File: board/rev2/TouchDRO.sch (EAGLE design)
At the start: 27 parts

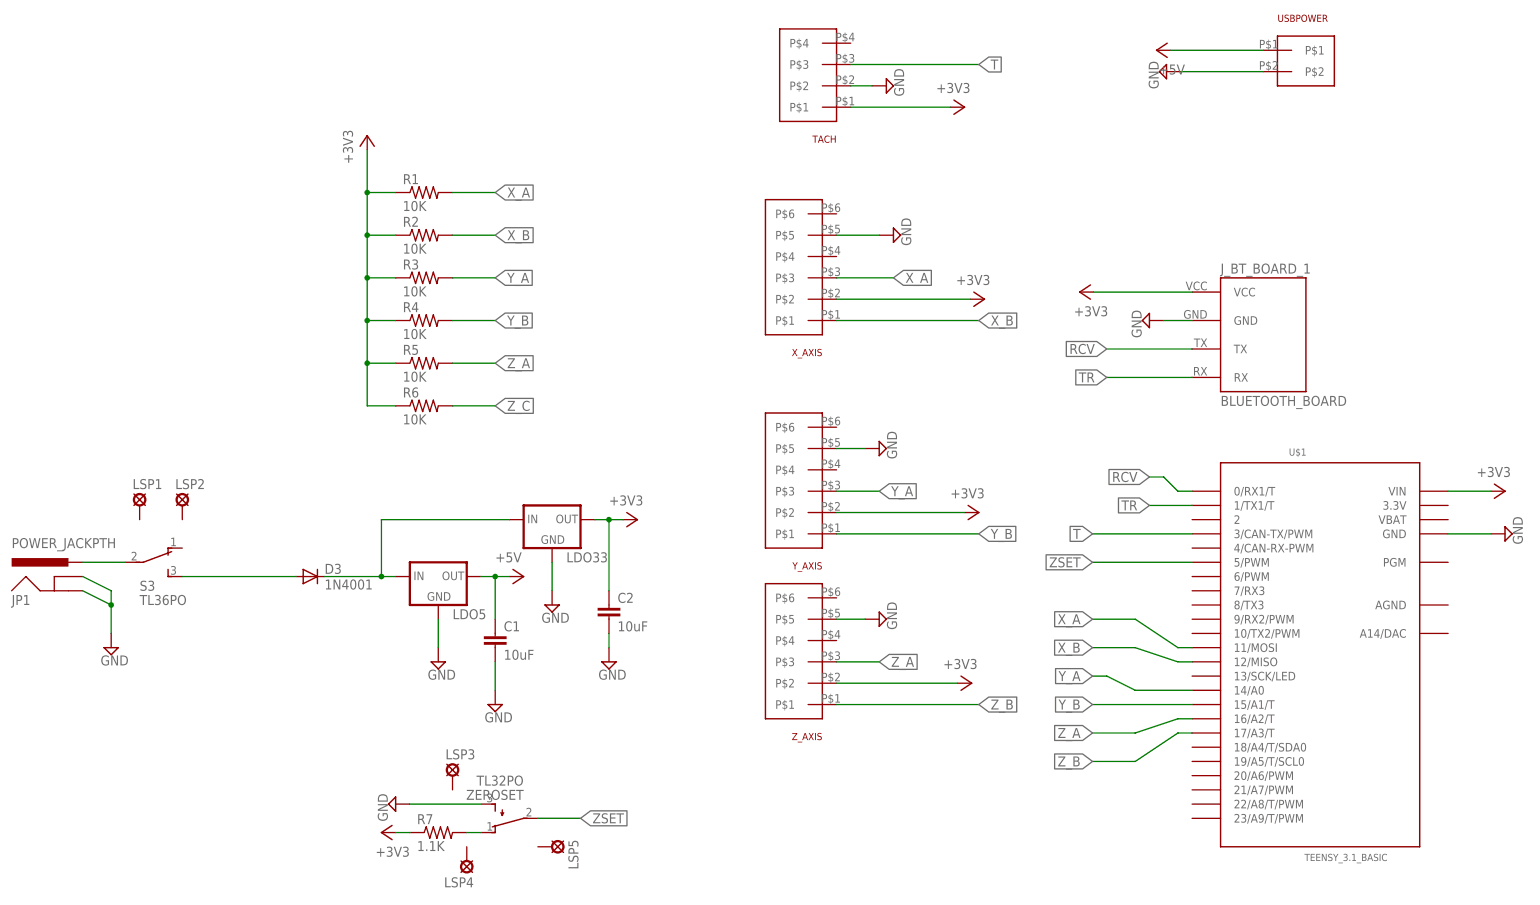
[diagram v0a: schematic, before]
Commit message: adding rev2 dependencies and updates to the rev2 board
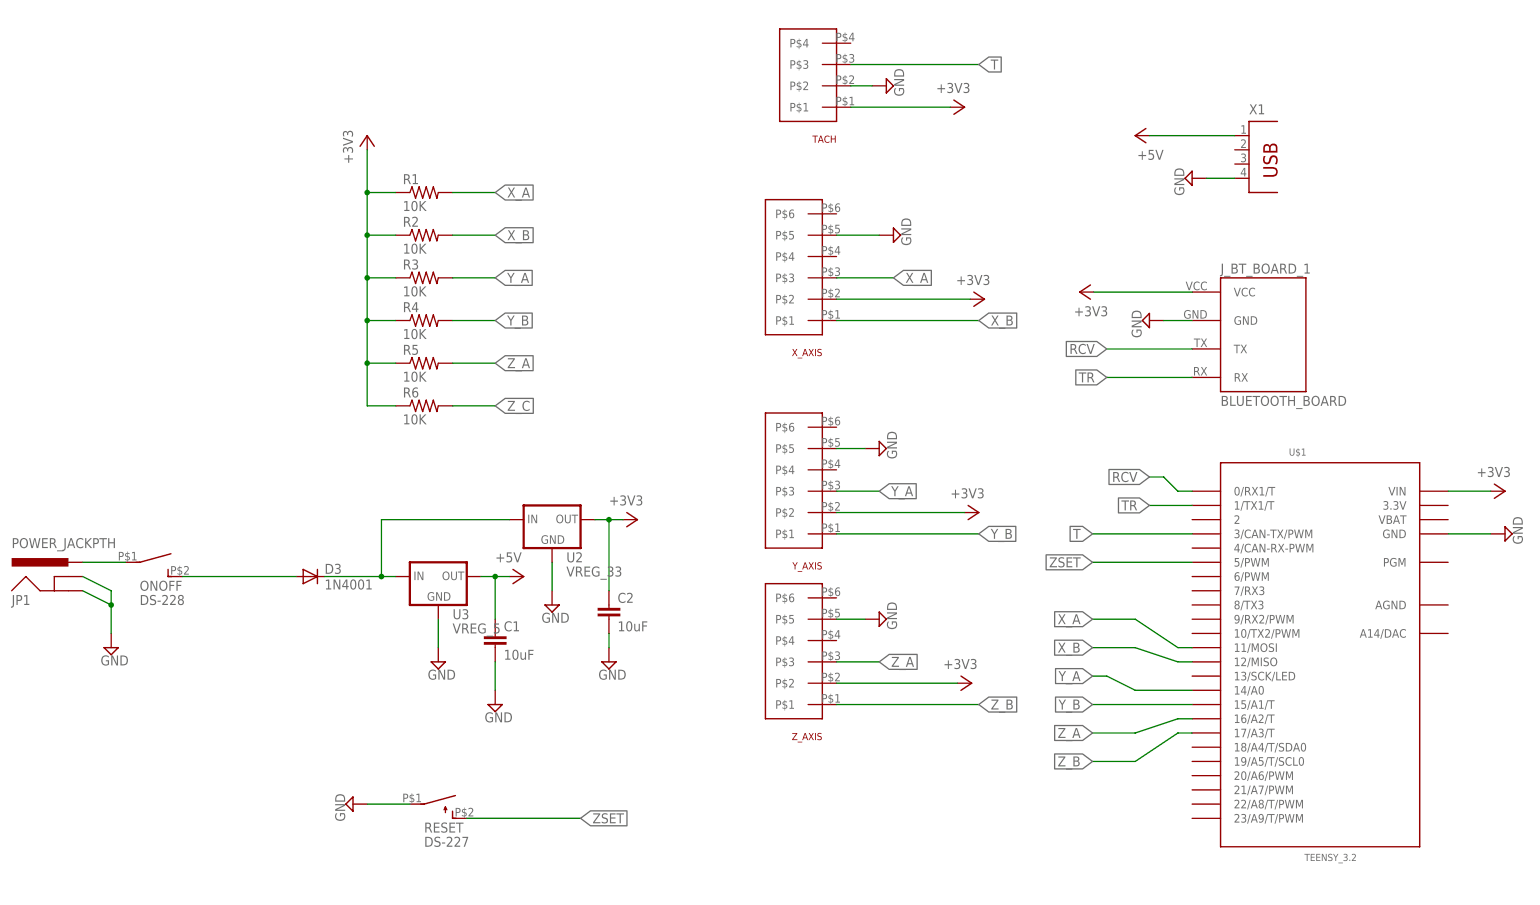
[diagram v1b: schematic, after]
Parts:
- removed LDO33, LDO5: (no value), SparkFun-PowerIC:V_REG_78XXSINK
- removed LSP1, LSP2, LSP3, LSP4, LSP5: LSP13, solpad:LSP13
- removed R7: 1.1K, SparkFun-Passives:RESISTOREZ
- removed S3: TL36PO, switch:TL36PO
- removed USBPOWER: KF2510_2PIN, KF2510:KF2510_2PIN
- removed ZEROSET: TL32PO, switch:TL32PO
- added ONOFF: DS-228, Switches:DS-228
- added RESET: DS-227, Switches:DS-227
- added U2: VREG_33, regulators:VREG_33
- added U3: VREG_5, regulators:VREG_5
- added X1: (no value), con-berg:PN87520
- U$1: value TEENSY_3.1_BASIC -> TEENSY_3.2
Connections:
- removed net N$2: R7.2, ZEROSET.O
- net +3V3: now also U2.OUT; no longer LDO33.OUT, R7.1
- net +5V: now also U3.OUT, X1.1; no longer LDO5.OUT, USBPOWER.P$1
- net D1: now also U2.IN, U3.IN; no longer LDO33.IN, LDO5.IN
- net GND: now also RESET.P, U2.GND, U3.GND, X1.4; no longer LDO33.GND, LDO5.GND, USBPOWER.P$2, ZEROSET.S
- net N$6: now also ONOFF.P; no longer S3.P
- net ONOFF: now also ONOFF.S; no longer S3.S
- net ZSET: now also RESET.S; no longer ZEROSET.P
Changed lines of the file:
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@@
 <part name="SUPPLY2" library="supply2" deviceset="GND" device=""/>
 <part name="J_BT_BOARD_1" library="Bluetooth HC-05" deviceset="BLUETOOTH_BOARD" device=""/>
-<part name="U$1" library="Teensy_3_Series_Board_v1.0" deviceset="TEENSY_3.1_BASIC" device=""/>
+<part name="U$1" library="Teensy_3_Series_Board_v1.0" deviceset="TEENSY_3.1_BASIC" device="" value="TEENSY_3.2"/>
 <part name="SUPPLY5" library="supply2" deviceset="GND" device=""/>
 <part name="SUPPLY7" library="supply2" deviceset="GND" device=""/>
@@
 <part name="SUPPLY16" library="supply2" deviceset="GND" device=""/>
 <part name="SUPPLY18" library="supply2" deviceset="GND" device=""/>
-<part name="USBPOWER" library="KF2510" deviceset="KF2510_2PIN" device=""/>
 <part name="SUPPLY20" library="supply2" deviceset="GND" device=""/>
 <part name="P+2" library="supply1" deviceset="+5V" device=""/>
@@
 <part name="C2" library="SparkFun-Passives" deviceset="CAP" device="EZ" value="10uF"/>
 <part name="SUPPLY1" library="supply2" deviceset="GND" device=""/>
-<part name="LDO5" library="SparkFun-PowerIC" deviceset="V_REG_78XX" device="SINK"/>
-<part name="LDO33" library="SparkFun-PowerIC" deviceset="V_REG_78XX" device="SINK"/>
 <part name="+3V1" library="supply1" deviceset="+3V3" device=""/>
 <part name="+3V2" library="supply1" deviceset="+3V3" device=""/>
 <part name="P+1" library="supply1" deviceset="+5V" device=""/>
-<part name="ZEROSET" library="switch" deviceset="TL32PO" device=""/>
-<part name="S3" library="switch" deviceset="TL36PO" device=""/>
 <part name="SUPPLY3" library="supply2" deviceset="GND" device=""/>
-<part name="+3V7" library="supply1" deviceset="+3V3" device=""/>
 <part name="R1" library="SparkFun-Passives" deviceset="RESISTOR" device="EZ" value="10K"/>
 <part name="R2" library="SparkFun-Passives" deviceset="RESISTOR" device="EZ" value="10K"/>
@@
 <part name="R5" library="SparkFun-Passives" deviceset="RESISTOR" device="EZ" value="10K"/>
 <part name="R6" library="SparkFun-Passives" deviceset="RESISTOR" device="EZ" value="10K"/>
-<part name="R7" library="SparkFun-Passives" deviceset="RESISTOR" device="EZ" value="1.1K"/>
-<part name="LSP1" library="solpad" deviceset="LSP13" device=""/>
-<part name="LSP2" library="solpad" deviceset="LSP13" device=""/>
-<part name="LSP3" library="solpad" deviceset="LSP13" device=""/>
-<part name="LSP4" library="solpad" deviceset="LSP13" device=""/>
-<part name="LSP5" library="solpad" deviceset="LSP13" device=""/>
+<part name="RESET" library="Switches" deviceset="DS-227" device=""/>
+<part name="ONOFF" library="Switches" deviceset="DS-228" device=""/>
+<part name="X1" library="con-berg" deviceset="PN87520" device=""/>
+<part name="U2" library="regulators" deviceset="VREG_33" device=""/>
+<part name="U3" library="regulators" deviceset="VREG_5" device=""/>
 </parts>
 <sheets>
@@
 <instance part="SUPPLY16" gate="GND" x="-68.58" y="-27.94"/>
 <instance part="SUPPLY18" gate="GND" x="-78.74" y="-20.32"/>
-<instance part="USBPOWER" gate="G$1" x="71.12" y="91.44"/>
-<instance part="SUPPLY20" gate="GND" x="51.308" y="85.09" rot="R270"/>
+<instance part="SUPPLY20" gate="GND" x="55.88" y="66.04" rot="R270"/>
 <instance part="P+2" gate="1" x="-63.5" y="-5.08" rot="R270"/>
 <instance part="+3V3" gate="G$1" x="-43.18" y="5.08" rot="R270"/>
@@
 <instance part="C2" gate="G$1" x="-48.26" y="-12.7"/>
 <instance part="SUPPLY1" gate="GND" x="-48.26" y="-20.32"/>
-<instance part="LDO5" gate="G$1" x="-78.74" y="-5.08"/>
-<instance part="LDO33" gate="G$1" x="-58.42" y="5.08"/>
 <instance part="+3V1" gate="G$1" x="35.814" y="45.72" rot="R90"/>
 <instance part="+3V2" gate="G$1" x="-91.44" y="73.66"/>
-<instance part="P+1" gate="1" x="49.53" y="88.9" rot="R90"/>
-<instance part="ZEROSET" gate="BEF1" x="-66.04" y="-48.26" rot="R90"/>
-<instance part="S3" gate="BEF1" x="-129.54" y="-2.54" rot="R270"/>
-<instance part="SUPPLY3" gate="GND" x="-86.36" y="-45.72" rot="R270"/>
-<instance part="+3V7" gate="G$1" x="-88.9" y="-50.8" rot="R90"/>
+<instance part="P+1" gate="1" x="45.72" y="73.66" rot="R90"/>
+<instance part="SUPPLY3" gate="GND" x="-93.98" y="-45.72" rot="R270"/>
 <instance part="R1" gate="G$1" x="-81.28" y="63.5"/>
 <instance part="R2" gate="G$1" x="-81.28" y="55.88"/>
@@
 <instance part="R5" gate="G$1" x="-81.28" y="33.02"/>
 <instance part="R6" gate="G$1" x="-81.28" y="25.4"/>
-<instance part="R7" gate="G$1" x="-78.74" y="-50.8"/>
-<instance part="LSP1" gate="1" x="-132.08" y="7.62"/>
-<instance part="LSP2" gate="1" x="-124.46" y="7.62"/>
-<instance part="LSP3" gate="1" x="-76.2" y="-40.64"/>
-<instance part="LSP4" gate="1" x="-73.66" y="-55.88" rot="R180"/>
-<instance part="LSP5" gate="1" x="-58.42" y="-53.34" rot="R270"/>
+<instance part="RESET" gate="G$1" x="-78.74" y="-45.72" rot="R270"/>
+<instance part="ONOFF" gate="G$1" x="-129.54" y="-2.54" rot="R270"/>
+<instance part="X1" gate="G$1" x="66.04" y="68.58"/>
+<instance part="U2" gate="G$1" x="-58.42" y="5.08"/>
+<instance part="U3" gate="G$1" x="-78.74" y="-5.08"/>
 </instances>
 <busses>
@@
 </segment>
 <segment>
-<pinref part="USBPOWER" gate="G$1" pin="P$2"/>
-<wire x1="68.58" y1="85.09" x2="53.848" y2="85.09" width="0.1524" layer="91"/>
-<pinref part="SUPPLY20" gate="GND" pin="GND"/>
-</segment>
-<segment>
 <pinref part="SUPPLY1" gate="GND" pin="GND"/>
 <pinref part="C2" gate="G$1" pin="2"/>
@@
 </segment>
 <segment>
-<pinref part="LDO33" gate="G$1" pin="GND"/>
 <pinref part="SUPPLY15" gate="GND" pin="GND"/>
 <wire x1="-58.42" y1="-2.54" x2="-58.42" y2="-7.62" width="0.1524" layer="91"/>
+<pinref part="U2" gate="G$1" pin="GND"/>
 </segment>
 <segment>
 <pinref part="SUPPLY18" gate="GND" pin="GND"/>
-<pinref part="LDO5" gate="G$1" pin="GND"/>
 <wire x1="-78.74" y1="-17.78" x2="-78.74" y2="-12.7" width="0.1524" layer="91"/>
-</segment>
-<segment>
-<pinref part="ZEROSET" gate="BEF1" pin="S"/>
-<wire x1="-71.12" y1="-45.72" x2="-83.82" y2="-45.72" width="0.1524" layer="91"/>
+<pinref part="U3" gate="G$1" pin="GND"/>
+</segment>
+<segment>
 <pinref part="SUPPLY3" gate="GND" pin="GND"/>
+<pinref part="RESET" gate="G$1" pin="P"/>
+<wire x1="-91.44" y1="-45.72" x2="-83.82" y2="-45.72" width="0.1524" layer="91"/>
+</segment>
+<segment>
+<pinref part="X1" gate="G$1" pin="4"/>
+<wire x1="63.5" y1="66.04" x2="58.42" y2="66.04" width="0.1524" layer="91"/>
+<pinref part="SUPPLY20" gate="GND" pin="GND"/>
 </segment>
 </net>
@@
 <pinref part="JP1" gate="G$1" pin="PWR"/>
 <wire x1="-142.24" y1="-2.54" x2="-134.62" y2="-2.54" width="0.1524" layer="91"/>
-<pinref part="S3" gate="BEF1" pin="P"/>
+<pinref part="ONOFF" gate="G$1" pin="P"/>
 </segment>
 </net>
@@
 <pinref part="D3" gate="G$1" pin="A"/>
 <wire x1="-124.46" y1="-5.08" x2="-104.14" y2="-5.08" width="0.1524" layer="91"/>
-<pinref part="S3" gate="BEF1" pin="S"/>
+<pinref part="ONOFF" gate="G$1" pin="S"/>
 </segment>
 </net>
 <net name="+5V" class="0">
 <segment>
-<pinref part="LDO5" gate="G$1" pin="OUT"/>
 <pinref part="P+2" gate="1" pin="+5V"/>
 <wire x1="-71.12" y1="-5.08" x2="-68.58" y2="-5.08" width="0.1524" layer="91"/>
@@
 <pinref part="C1" gate="G$1" pin="1"/>
 <wire x1="-68.58" y1="-5.08" x2="-68.58" y2="-12.7" width="0.1524" layer="91"/>
-</segment>
-<segment>
-<pinref part="USBPOWER" gate="G$1" pin="P$1"/>
-<wire x1="68.58" y1="88.9" x2="52.07" y2="88.9" width="0.1524" layer="91"/>
+<pinref part="U3" gate="G$1" pin="OUT"/>
+</segment>
+<segment>
+<pinref part="X1" gate="G$1" pin="1"/>
+<wire x1="48.26" y1="73.66" x2="63.5" y2="73.66" width="0.1524" layer="91"/>
 <pinref part="P+1" gate="1" pin="+5V"/>
 </segment>
@@
 </segment>
 <segment>
-<pinref part="LDO33" gate="G$1" pin="OUT"/>
 <pinref part="+3V3" gate="G$1" pin="+3V3"/>
 <wire x1="-50.8" y1="5.08" x2="-48.26" y2="5.08" width="0.1524" layer="91"/>
@@
 <pinref part="C2" gate="G$1" pin="1"/>
 <wire x1="-48.26" y1="5.08" x2="-48.26" y2="-7.62" width="0.1524" layer="91"/>
+<pinref part="U2" gate="G$1" pin="OUT"/>
 </segment>
 <segment>
@@
 <pinref part="R6" gate="G$1" pin="1"/>
 </segment>
-<segment>
-<pinref part="+3V7" gate="G$1" pin="+3V3"/>
-<wire x1="-86.36" y1="-50.8" x2="-83.82" y2="-50.8" width="0.1524" layer="91"/>
-<pinref part="R7" gate="G$1" pin="1"/>
-</segment>
 </net>
 <net name="D1" class="0">
 <segment>
-<pinref part="LDO5" gate="G$1" pin="IN"/>
 <wire x1="-88.9" y1="-5.08" x2="-86.36" y2="-5.08" width="0.1524" layer="91"/>
 <wire x1="-88.9" y1="-5.08" x2="-88.9" y2="5.08" width="0.1524" layer="91"/>
-<pinref part="LDO33" gate="G$1" pin="IN"/>
 <wire x1="-88.9" y1="5.08" x2="-66.04" y2="5.08" width="0.1524" layer="91"/>
 <pinref part="D3" gate="G$1" pin="C"/>
 <wire x1="-99.06" y1="-5.08" x2="-88.9" y2="-5.08" width="0.1524" layer="91"/>
 <junction x="-88.9" y="-5.08"/>
+<pinref part="U2" gate="G$1" pin="IN"/>
+<pinref part="U3" gate="G$1" pin="IN"/>
 </segment>
 </net>
@@
 </segment>
 <segment>
-<pinref part="ZEROSET" gate="BEF1" pin="P"/>
-<wire x1="-60.96" y1="-48.26" x2="-53.34" y2="-48.26" width="0.1524" layer="91"/>
+<wire x1="-73.66" y1="-48.26" x2="-53.34" y2="-48.26" width="0.1524" layer="91"/>
 <label x="-53.34" y="-48.26" size="1.778" layer="95" xref="yes"/>
-</segment>
-</net>
-<net name="N$2" class="0">
-<segment>
-<pinref part="ZEROSET" gate="BEF1" pin="O"/>
-<wire x1="-73.66" y1="-50.8" x2="-71.12" y2="-50.8" width="0.1524" layer="91"/>
-<pinref part="R7" gate="G$1" pin="2"/>
-</segment>
-</net>
+<pinref part="RESET" gate="G$1" pin="S"/>
+</segment>
+</net>

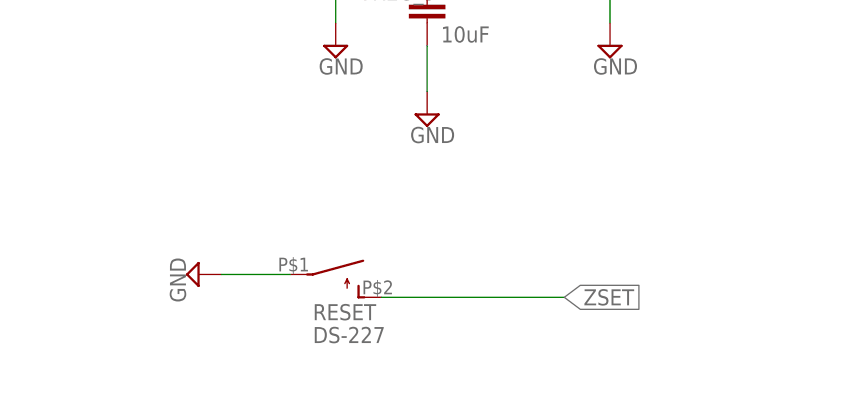
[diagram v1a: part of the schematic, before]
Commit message: tweaks to board and layout. added dxf output of board layout
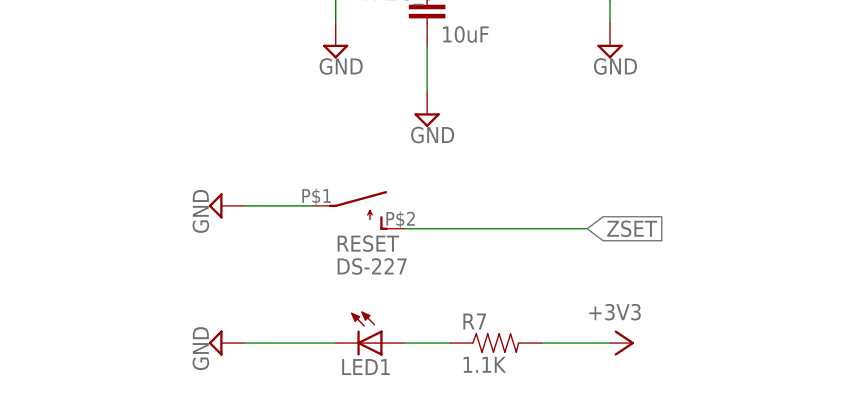
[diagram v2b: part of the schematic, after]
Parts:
- added LED1: (no value), led:LED3MM
- added R7: 1.1K, SparkFun-Passives:RESISTOREZ
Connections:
- new net N$1: LED1.A, R7.1
- net +3V3: now also R7.2
- net GND: now also LED1.C
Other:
- moved on the sheet: RESET
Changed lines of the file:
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@@
 <part name="U2" library="regulators" deviceset="VREG_33" device=""/>
 <part name="U3" library="regulators" deviceset="VREG_5" device=""/>
+<part name="LED1" library="led" deviceset="LED" device="3MM"/>
+<part name="SUPPLY4" library="supply2" deviceset="GND" device=""/>
+<part name="+3V7" library="supply1" deviceset="+3V3" device=""/>
+<part name="R7" library="SparkFun-Passives" deviceset="RESISTOR" device="EZ" value="1.1K"/>
 </parts>
 <sheets>
@@
 <instance part="+3V2" gate="G$1" x="-91.44" y="73.66"/>
 <instance part="P+1" gate="1" x="45.72" y="73.66" rot="R90"/>
-<instance part="SUPPLY3" gate="GND" x="-93.98" y="-45.72" rot="R270"/>
+<instance part="SUPPLY3" gate="GND" x="-91.44" y="-38.1" rot="R270"/>
 <instance part="R1" gate="G$1" x="-81.28" y="63.5"/>
 <instance part="R2" gate="G$1" x="-81.28" y="55.88"/>
@@
 <instance part="R5" gate="G$1" x="-81.28" y="33.02"/>
 <instance part="R6" gate="G$1" x="-81.28" y="25.4"/>
-<instance part="RESET" gate="G$1" x="-78.74" y="-45.72" rot="R270"/>
+<instance part="RESET" gate="G$1" x="-76.2" y="-38.1" rot="R270"/>
 <instance part="ONOFF" gate="G$1" x="-129.54" y="-2.54" rot="R270"/>
 <instance part="X1" gate="G$1" x="66.04" y="68.58"/>
 <instance part="U2" gate="G$1" x="-58.42" y="5.08"/>
 <instance part="U3" gate="G$1" x="-78.74" y="-5.08"/>
+<instance part="LED1" gate="G$1" x="-73.66" y="-53.34" rot="R270"/>
+<instance part="SUPPLY4" gate="GND" x="-91.44" y="-53.34" rot="R270"/>
+<instance part="+3V7" gate="G$1" x="-45.72" y="-53.34" rot="R270"/>
+<instance part="R7" gate="G$1" x="-60.96" y="-53.34"/>
 </instances>
 <busses>
@@
 <pinref part="SUPPLY3" gate="GND" pin="GND"/>
 <pinref part="RESET" gate="G$1" pin="P"/>
-<wire x1="-91.44" y1="-45.72" x2="-83.82" y2="-45.72" width="0.1524" layer="91"/>
+<wire x1="-88.9" y1="-38.1" x2="-81.28" y2="-38.1" width="0.1524" layer="91"/>
 </segment>
 <segment>
@@
 <wire x1="63.5" y1="66.04" x2="58.42" y2="66.04" width="0.1524" layer="91"/>
 <pinref part="SUPPLY20" gate="GND" pin="GND"/>
+</segment>
+<segment>
+<pinref part="SUPPLY4" gate="GND" pin="GND"/>
+<pinref part="LED1" gate="G$1" pin="C"/>
+<wire x1="-88.9" y1="-53.34" x2="-78.74" y2="-53.34" width="0.1524" layer="91"/>
 </segment>
 </net>
@@
 <pinref part="R6" gate="G$1" pin="1"/>
 </segment>
+<segment>
+<pinref part="R7" gate="G$1" pin="2"/>
+<pinref part="+3V7" gate="G$1" pin="+3V3"/>
+<wire x1="-55.88" y1="-53.34" x2="-48.26" y2="-53.34" width="0.1524" layer="91"/>
+</segment>
 </net>
 <net name="D1" class="0">
@@
 </segment>
 <segment>
-<wire x1="-73.66" y1="-48.26" x2="-53.34" y2="-48.26" width="0.1524" layer="91"/>
-<label x="-53.34" y="-48.26" size="1.778" layer="95" xref="yes"/>
+<wire x1="-71.12" y1="-40.64" x2="-50.8" y2="-40.64" width="0.1524" layer="91"/>
+<label x="-50.8" y="-40.64" size="1.778" layer="95" xref="yes"/>
 <pinref part="RESET" gate="G$1" pin="S"/>
 </segment>
 </net>
+<net name="N$1" class="0">
+<segment>
+<pinref part="LED1" gate="G$1" pin="A"/>
+<pinref part="R7" gate="G$1" pin="1"/>
+<wire x1="-71.12" y1="-53.34" x2="-66.04" y2="-53.34" width="0.1524" layer="91"/>
+</segment>
+</net>
